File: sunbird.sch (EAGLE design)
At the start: 41 parts, among them J1 USB_MINI-B_SMT, Q1 600mA/40V, U1000 TP4056, U1500 FS312F-G, U1550 FS8205, U2000 MT3608, U4000 FM116B, U5000 CH340G, Y5000 12Mhz

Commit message: Getting there
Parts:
- removed R2003: 4.5k, rcl:R-EU_R0603
- added D2003: DIODE-SCHOTTKY-PMEG4005EJ, SparkFun-DiscreteSemi:DIODE-SCHOTTKY-PMEG4005EJ
- added R2005: 1k, rcl:R-EU_R0603
- R2004: value 1k -> 4.5k
- renumbered C2005 to C2006, C3 to C8008, MDL1 to U8000, Q1 to Q8010, R10 to R8003, R11 to R8004, R12 to R8005, R13 to R8006, R8 to R8001, R9 to R8002
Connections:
- net N$14 renamed MOTOR_A
- net N$15 renamed MOTOR_B
- net SDA renamed GPIO4
- removed net SCL: U8000.GPIO5
- removed net USB_D+: U5000.D+
- removed net USB_D-: U5000.D-
- new net GPIO5: Q8010.B, U8000.GPIO5
- net 3.3V: now also D2003.C, R2004.2; no longer R2003.2
- net GND: now also R2005.1; no longer R2004.1
- net GPIO16: no longer Q8010.B
- net N$12: now also D2003.A
- net N$13: now also R2004.1, R2005.2; no longer R2003.1, R2004.2
- net USB_N: now also U5000.D-
- net USB_P: now also U5000.D+

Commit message: Almost done
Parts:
- removed J2: (no value), SparkFun-Connectors:CONN_03X2SHROUD
- added U$1: ESP8266_PROGRAMMER, geusebio:ESP8266_PROGRAMMER
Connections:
- net 3.3V: now also U$1.VCC; no longer J2.1
- net GND: now also U$1.GND; no longer J2.6
- net GPIO0: now also U$1.GPIO0; no longer J2.4
- net RESET: now also U$1.RESET; no longer J2.2
- net RX: now also U$1.RX; no longer J2.3
- net TX: now also U$1.TX; no longer J2.5
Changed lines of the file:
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@@
 <part name="R8004" library="rcl" library_urn="urn:adsk.eagle:library:334" deviceset="R-EU_" device="R0603" value="10k"/>
 <part name="LOGO1" library="SparkFun-Aesthetics" deviceset="OSHW-LOGO" device="S"/>
-<part name="J2" library="SparkFun-Connectors" deviceset="CONN_03X2" device="SHROUD"/>
 <part name="SUPPLY16" library="SparkFun-PowerSymbols" library_urn="urn:adsk.eagle:library:530" deviceset="3.3V" device=""/>
 <part name="GND17" library="SparkFun-PowerSymbols" library_urn="urn:adsk.eagle:library:530" deviceset="GND" device=""/>
@@
 <part name="C4001" library="rcl" library_urn="urn:adsk.eagle:library:334" deviceset="C-EU" device="C0603" package3d_urn="urn:adsk.eagle:package:23616/2"/>
 <part name="D2003" library="SparkFun-DiscreteSemi" library_urn="urn:adsk.eagle:library:514" deviceset="DIODE-SCHOTTKY" device="-PMEG4005EJ" package3d_urn="urn:adsk.eagle:package:38441/1" value=""/>
+<part name="U$1" library="geusebio" deviceset="ESP8266_PROGRAMMER" device=""/>
 </parts>
 <sheets>
@@
 <instance part="R8004" gate="G$1" x="144.78" y="48.26"/>
 <instance part="LOGO1" gate="G$1" x="124.46" y="15.24"/>
-<instance part="J2" gate="G$1" x="81.28" y="50.8"/>
-<instance part="SUPPLY16" gate="G$1" x="71.12" y="55.88"/>
-<instance part="GND17" gate="1" x="91.44" y="43.18"/>
+<instance part="SUPPLY16" gate="G$1" x="30.48" y="58.42"/>
+<instance part="GND17" gate="1" x="30.48" y="33.02"/>
 <instance part="R8005" gate="G$1" x="30.48" y="96.52" rot="R90"/>
 <instance part="R8006" gate="G$1" x="30.48" y="81.28" rot="R90"/>
@@
 <instance part="SUPPLY17" gate="G$1" x="30.48" y="119.38"/>
 <instance part="Q8010" gate="G$1" x="33.02" y="109.22" rot="MR0"/>
+<instance part="U$1" gate="G$1" x="15.24" y="45.72"/>
 </instances>
 <busses>
@@
 </segment>
 <segment>
-<pinref part="J2" gate="G$1" pin="3"/>
-<wire x1="73.66" y1="50.8" x2="71.12" y2="50.8" width="0.1524" layer="91"/>
-<label x="71.12" y="50.8" size="1.27" layer="95" rot="R180" xref="yes"/>
+<wire x1="27.94" y1="48.26" x2="30.48" y2="48.26" width="0.1524" layer="91"/>
+<label x="30.48" y="48.26" size="1.27" layer="95" xref="yes"/>
+<pinref part="U$1" gate="G$1" pin="RX"/>
 </segment>
 </net>
@@
 </segment>
 <segment>
-<pinref part="J2" gate="G$1" pin="2"/>
-<wire x1="88.9" y1="53.34" x2="91.44" y2="53.34" width="0.1524" layer="91"/>
-<label x="91.44" y="53.34" size="1.27" layer="95" xref="yes"/>
+<wire x1="27.94" y1="50.8" x2="30.48" y2="50.8" width="0.1524" layer="91"/>
+<label x="30.48" y="50.8" size="1.27" layer="95" xref="yes"/>
+<pinref part="U$1" gate="G$1" pin="RESET"/>
 </segment>
 </net>
@@
 </segment>
 <segment>
-<pinref part="J2" gate="G$1" pin="1"/>
-<wire x1="73.66" y1="53.34" x2="71.12" y2="53.34" width="0.1524" layer="91"/>
-<wire x1="71.12" y1="53.34" x2="71.12" y2="55.88" width="0.1524" layer="91"/>
+<wire x1="27.94" y1="55.88" x2="30.48" y2="55.88" width="0.1524" layer="91"/>
+<wire x1="30.48" y1="55.88" x2="30.48" y2="58.42" width="0.1524" layer="91"/>
 <pinref part="SUPPLY16" gate="G$1" pin="3.3V"/>
+<pinref part="U$1" gate="G$1" pin="VCC"/>
 </segment>
 </net>
@@
 </segment>
 <segment>
-<pinref part="J2" gate="G$1" pin="6"/>
-<wire x1="88.9" y1="48.26" x2="91.44" y2="48.26" width="0.1524" layer="91"/>
-<wire x1="91.44" y1="48.26" x2="91.44" y2="45.72" width="0.1524" layer="91"/>
+<wire x1="27.94" y1="38.1" x2="30.48" y2="38.1" width="0.1524" layer="91"/>
+<wire x1="30.48" y1="38.1" x2="30.48" y2="35.56" width="0.1524" layer="91"/>
 <pinref part="GND17" gate="1" pin="GND"/>
+<pinref part="U$1" gate="G$1" pin="GND"/>
 </segment>
 <segment>
@@
 </segment>
 <segment>
-<pinref part="J2" gate="G$1" pin="5"/>
-<wire x1="71.12" y1="48.26" x2="73.66" y2="48.26" width="0.1524" layer="91"/>
-<label x="71.12" y="48.26" size="1.27" layer="95" rot="R180" xref="yes"/>
+<wire x1="30.48" y1="45.72" x2="27.94" y2="45.72" width="0.1524" layer="91"/>
+<label x="30.48" y="45.72" size="1.27" layer="95" xref="yes"/>
+<pinref part="U$1" gate="G$1" pin="TX"/>
 </segment>
 </net>
@@
 </segment>
 <segment>
-<pinref part="J2" gate="G$1" pin="4"/>
-<wire x1="88.9" y1="50.8" x2="91.44" y2="50.8" width="0.1524" layer="91"/>
-<label x="91.44" y="50.8" size="1.27" layer="95" xref="yes"/>
-</segment>
-</net>
+<wire x1="27.94" y1="43.18" x2="30.48" y2="43.18" width="0.1524" layer="91"/>
+<label x="30.48" y="43.18" size="1.27" layer="95" xref="yes"/>
+<pinref part="U$1" gate="G$1" pin="GPIO0"/>
+</segment>
+</net>

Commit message: Sunbird. Again.
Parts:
- D1004: value red -> CHRG
- D1005: value green -> OK
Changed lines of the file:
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@@
 <part name="GND1" library="SparkFun-PowerSymbols" library_urn="urn:adsk.eagle:library:530" deviceset="GND" device=""/>
 <part name="GND2" library="SparkFun-PowerSymbols" library_urn="urn:adsk.eagle:library:530" deviceset="GND" device=""/>
-<part name="D1004" library="SparkFun-LED" library_urn="urn:adsk.eagle:library:529" deviceset="LED" device="0603" package3d_urn="urn:adsk.eagle:package:39354/1" value="red"/>
-<part name="D1005" library="SparkFun-LED" library_urn="urn:adsk.eagle:library:529" deviceset="LED" device="0603" package3d_urn="urn:adsk.eagle:package:39354/1" value="green"/>
+<part name="D1004" library="SparkFun-LED" library_urn="urn:adsk.eagle:library:529" deviceset="LED" device="0603" package3d_urn="urn:adsk.eagle:package:39354/1" value="CHRG"/>
+<part name="D1005" library="SparkFun-LED" library_urn="urn:adsk.eagle:library:529" deviceset="LED" device="0603" package3d_urn="urn:adsk.eagle:package:39354/1" value="OK"/>
 <part name="SUPPLY5" library="SparkFun-PowerSymbols" library_urn="urn:adsk.eagle:library:530" deviceset="V_BATT" device=""/>
 <part name="U1500" library="geusebio" deviceset="FS312F-G" device=""/>

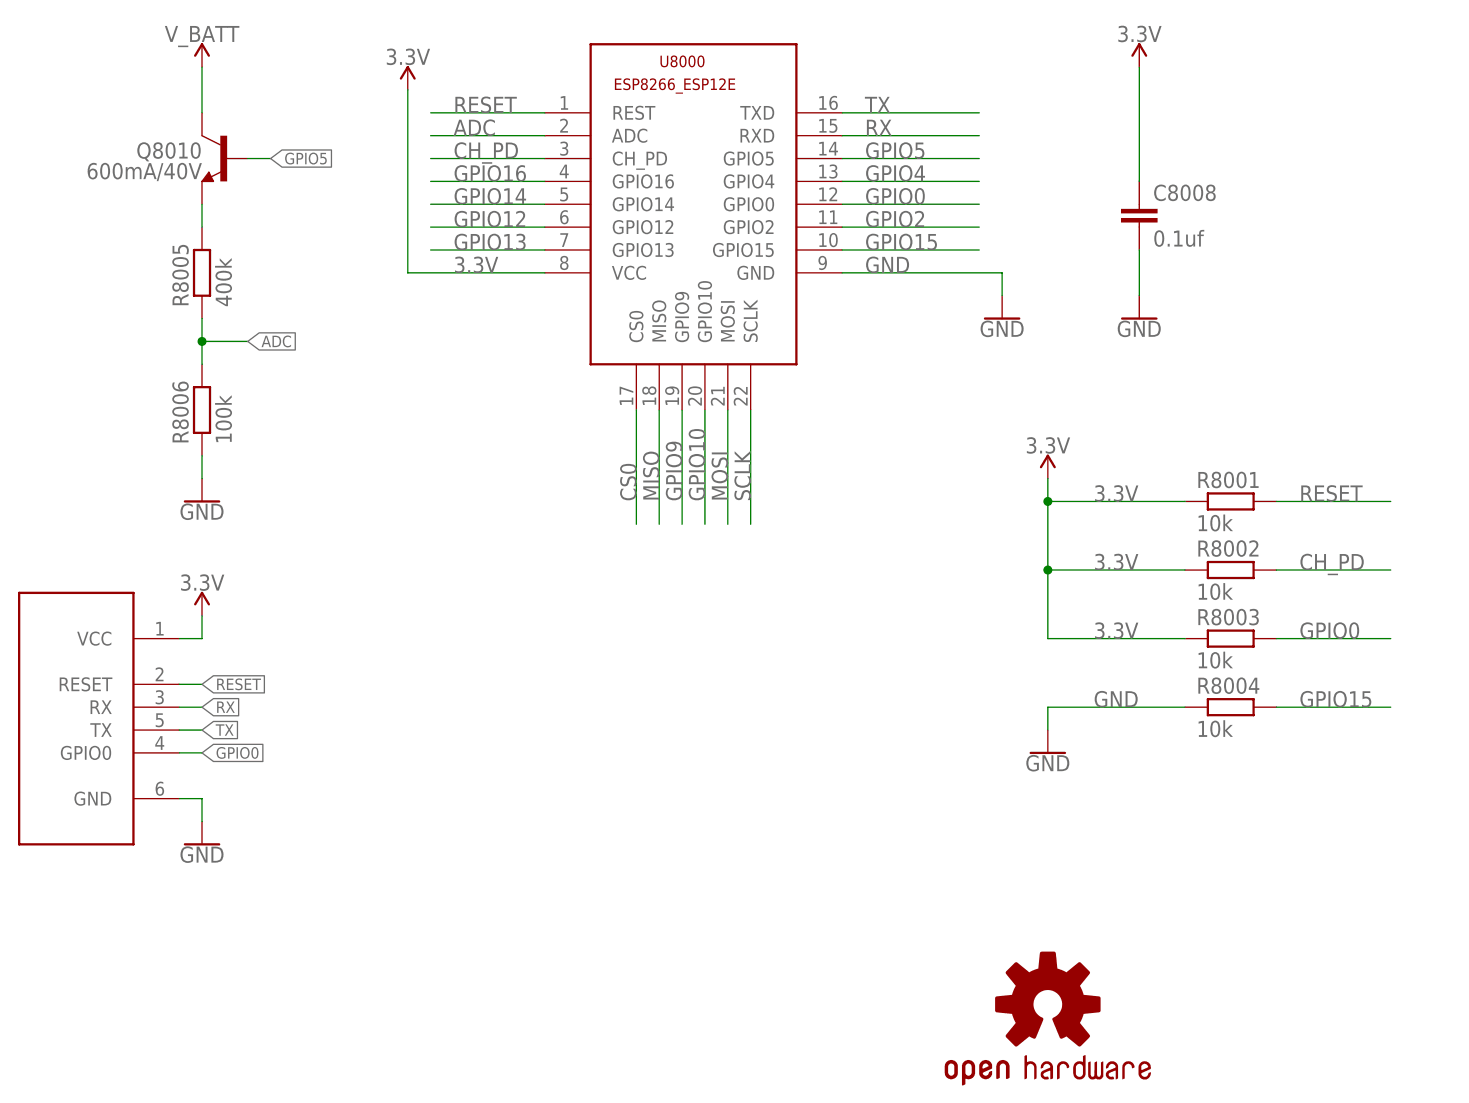
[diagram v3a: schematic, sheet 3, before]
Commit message: Add a status LED
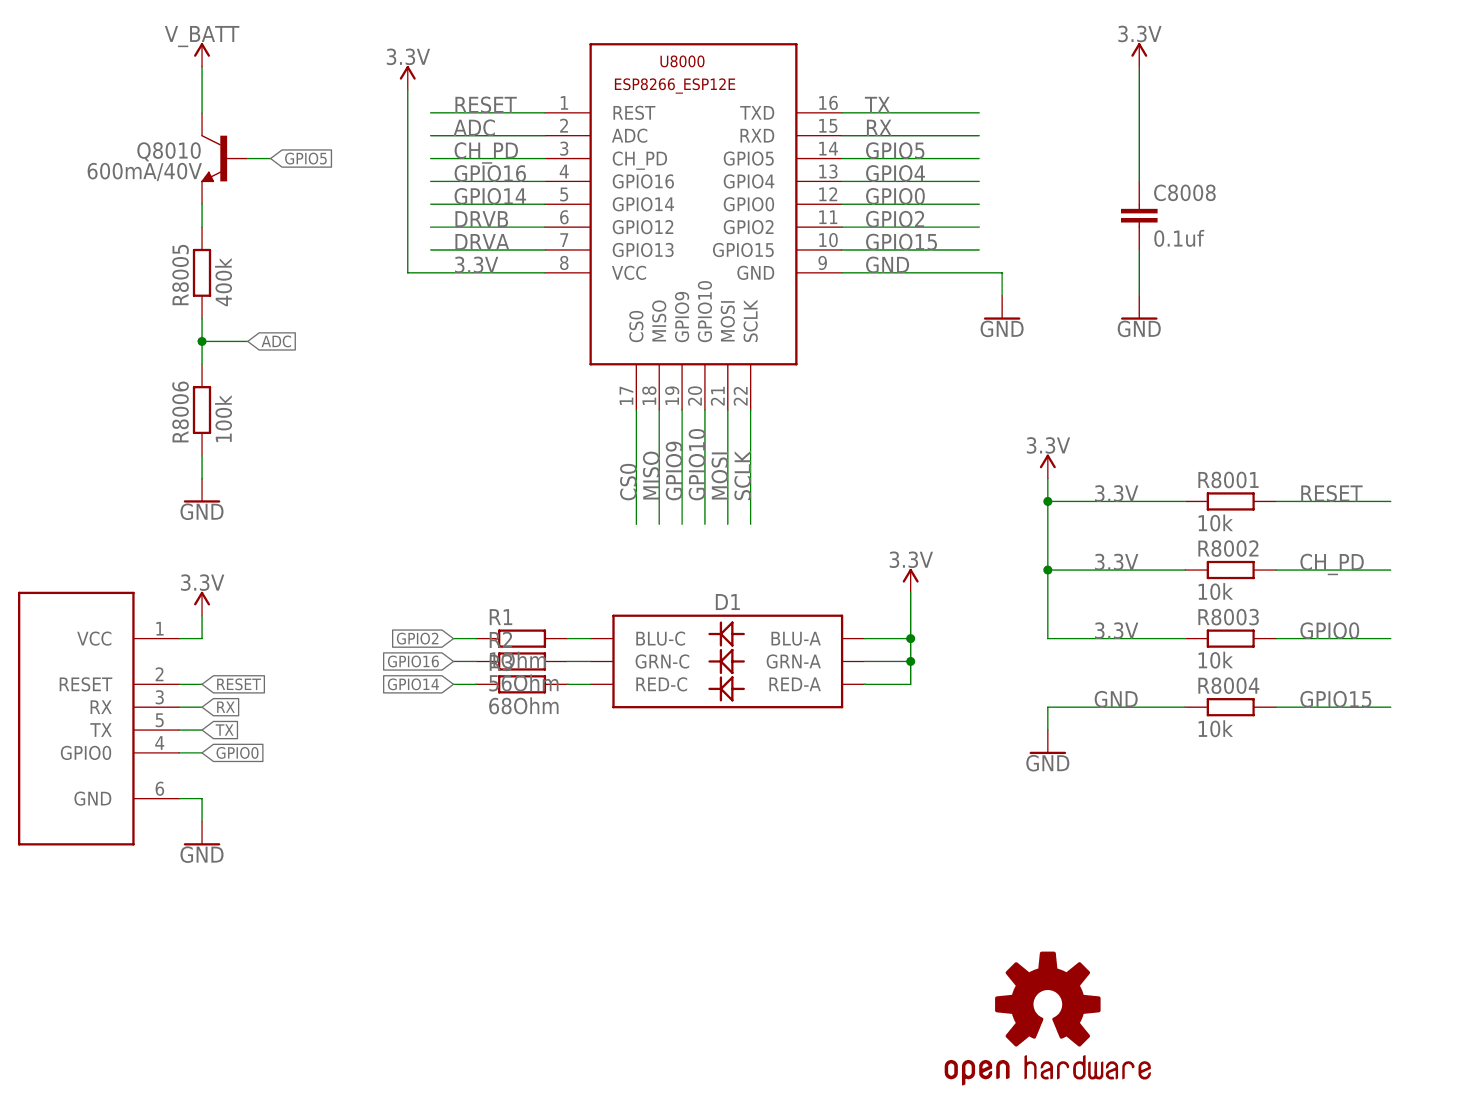
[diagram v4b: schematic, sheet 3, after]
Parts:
- added D1: (no value), SparkFun-LED:LED-RGBNO_IC
- added R1: 1Ohm, rcl:R-EU_R0603
- added R2: 56Ohm, rcl:R-EU_R0603
- added R3: 68Ohm, rcl:R-EU_R0603
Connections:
- net GPIO12 renamed DRVB
- net GPIO13 renamed DRVA
- new net N$14: D1.BLU-C, R1.2
- new net N$15: D1.GRN-C, R2.2
- new net N$16: D1.RED-C, R3.2
- net 3.3V: now also D1.BLU-A, D1.GRN-A, D1.RED-A
- net GPIO14: now also R3.1
- net GPIO16: now also R2.1
- net GPIO2: now also R1.1
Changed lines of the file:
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@@
 <part name="D2003" library="SparkFun-DiscreteSemi" library_urn="urn:adsk.eagle:library:514" deviceset="DIODE-SCHOTTKY" device="-PMEG4005EJ" package3d_urn="urn:adsk.eagle:package:38441/1" value=""/>
 <part name="U$1" library="geusebio" deviceset="ESP8266_PROGRAMMER" device=""/>
+<part name="D1" library="SparkFun-LED" library_urn="urn:adsk.eagle:library:529" deviceset="LED-RGB" device="NO_IC" package3d_urn="urn:adsk.eagle:package:39374/1"/>
+<part name="SUPPLY20" library="SparkFun-PowerSymbols" library_urn="urn:adsk.eagle:library:530" deviceset="3.3V" device=""/>
+<part name="R1" library="rcl" library_urn="urn:adsk.eagle:library:334" deviceset="R-EU_" device="R0603" value="1Ohm"/>
+<part name="R2" library="rcl" library_urn="urn:adsk.eagle:library:334" deviceset="R-EU_" device="R0603" value="56Ohm"/>
+<part name="R3" library="rcl" library_urn="urn:adsk.eagle:library:334" deviceset="R-EU_" device="R0603" value="68Ohm"/>
 </parts>
 <sheets>
@@
 <instance part="Q8010" gate="G$1" x="33.02" y="109.22" rot="MR0"/>
 <instance part="U$1" gate="G$1" x="15.24" y="45.72"/>
+<instance part="D1" gate="G$1" x="88.9" y="53.34" rot="MR0"/>
+<instance part="SUPPLY20" gate="G$1" x="109.22" y="60.96"/>
+<instance part="R1" gate="G$1" x="66.04" y="55.88"/>
+<instance part="R2" gate="G$1" x="66.04" y="53.34"/>
+<instance part="R3" gate="G$1" x="66.04" y="50.8"/>
 </instances>
 <busses>
 </busses>
 <nets>
-<net name="GPIO12" class="0">
+<net name="DRVB" class="0">
 <segment>
 <pinref part="U8000" gate="G$1" pin="GPIO12"/>
@@
 <wire x1="55.88" y1="106.68" x2="68.58" y2="106.68" width="0.1524" layer="91"/>
 <label x="58.42" y="106.68" size="1.778" layer="95"/>
+</segment>
+<segment>
+<pinref part="R2" gate="G$1" pin="1"/>
+<wire x1="58.42" y1="53.34" x2="60.96" y2="53.34" width="0.1524" layer="91"/>
+<label x="58.42" y="53.34" size="1.27" layer="95" rot="R180" xref="yes"/>
 </segment>
 </net>
@@
 <pinref part="U$1" gate="G$1" pin="VCC"/>
 </segment>
-</net>
-<net name="GPIO13" class="0">
+<segment>
+<pinref part="D1" gate="G$1" pin="BLU-A"/>
+<wire x1="104.14" y1="55.88" x2="109.22" y2="55.88" width="0.1524" layer="91"/>
+<pinref part="SUPPLY20" gate="G$1" pin="3.3V"/>
+<wire x1="109.22" y1="55.88" x2="109.22" y2="60.96" width="0.1524" layer="91"/>
+<pinref part="D1" gate="G$1" pin="GRN-A"/>
+<wire x1="104.14" y1="53.34" x2="109.22" y2="53.34" width="0.1524" layer="91"/>
+<wire x1="109.22" y1="53.34" x2="109.22" y2="55.88" width="0.1524" layer="91"/>
+<junction x="109.22" y="55.88"/>
+<pinref part="D1" gate="G$1" pin="RED-A"/>
+<wire x1="104.14" y1="50.8" x2="109.22" y2="50.8" width="0.1524" layer="91"/>
+<wire x1="109.22" y1="50.8" x2="109.22" y2="53.34" width="0.1524" layer="91"/>
+<junction x="109.22" y="53.34"/>
+</segment>
+</net>
+<net name="DRVA" class="0">
 <segment>
 <pinref part="U8000" gate="G$1" pin="GPIO13"/>
@@
 <wire x1="68.58" y1="104.14" x2="55.88" y2="104.14" width="0.1524" layer="91"/>
 <label x="58.42" y="104.14" size="1.778" layer="95"/>
+</segment>
+<segment>
+<pinref part="R3" gate="G$1" pin="1"/>
+<wire x1="60.96" y1="50.8" x2="58.42" y2="50.8" width="0.1524" layer="91"/>
+<label x="58.42" y="50.8" size="1.27" layer="95" rot="R180" xref="yes"/>
 </segment>
 </net>
@@
 <label x="104.14" y="101.6" size="1.778" layer="95"/>
 </segment>
+<segment>
+<pinref part="R1" gate="G$1" pin="1"/>
+<wire x1="60.96" y1="55.88" x2="58.42" y2="55.88" width="0.1524" layer="91"/>
+<label x="58.42" y="55.88" size="1.27" layer="95" rot="R180" xref="yes"/>
+</segment>
 </net>
 <net name="GPIO4" class="0">
@@
 <pinref part="R8005" gate="G$1" pin="2"/>
 <wire x1="30.48" y1="101.6" x2="30.48" y2="104.14" width="0.1524" layer="91"/>
+</segment>
+</net>
+<net name="N$14" class="0">
+<segment>
+<pinref part="R1" gate="G$1" pin="2"/>
+<pinref part="D1" gate="G$1" pin="BLU-C"/>
+<wire x1="71.12" y1="55.88" x2="73.66" y2="55.88" width="0.1524" layer="91"/>
+</segment>
+</net>
+<net name="N$15" class="0">
+<segment>
+<pinref part="D1" gate="G$1" pin="GRN-C"/>
+<pinref part="R2" gate="G$1" pin="2"/>
+<wire x1="73.66" y1="53.34" x2="71.12" y2="53.34" width="0.1524" layer="91"/>
+</segment>
+</net>
+<net name="N$16" class="0">
+<segment>
+<pinref part="R3" gate="G$1" pin="2"/>
+<pinref part="D1" gate="G$1" pin="RED-C"/>
+<wire x1="71.12" y1="50.8" x2="73.66" y2="50.8" width="0.1524" layer="91"/>
 </segment>
 </net>
@@
 </segment>
 </net>
-<net name="GPIO13" class="0">
+<net name="DRVA" class="0">
 <segment>
 <pinref part="U4000" gate="G$1" pin="IN1"/>
@@
 </segment>
 </net>
-<net name="GPIO12" class="0">
+<net name="DRVB" class="0">
 <segment>
 <pinref part="U4000" gate="G$1" pin="IN2"/>
